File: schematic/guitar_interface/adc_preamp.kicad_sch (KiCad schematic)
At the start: 17 parts, among them U6 OPA4134

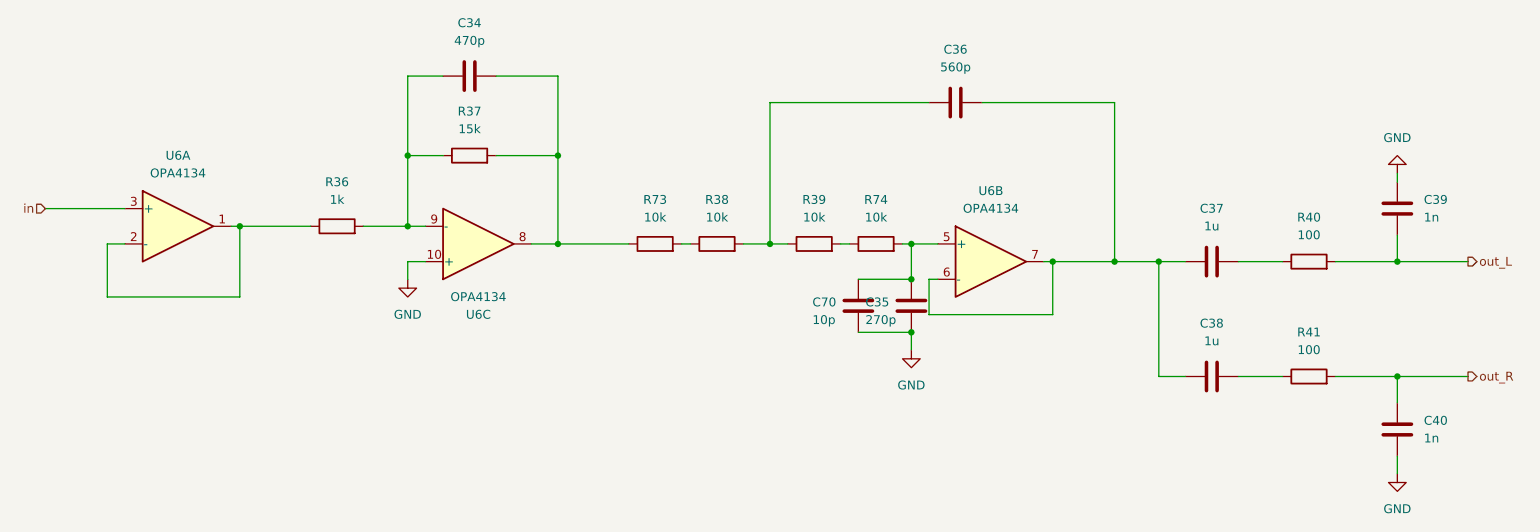
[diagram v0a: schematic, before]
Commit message: first scetch of audio pipeline and power supply layout
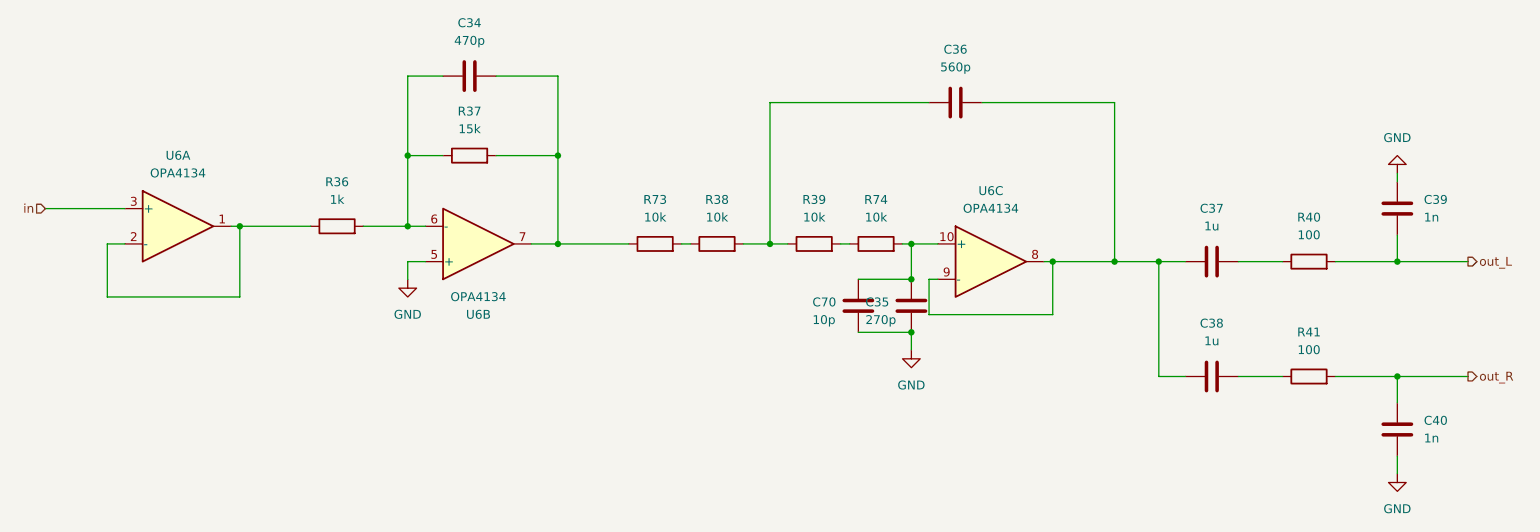
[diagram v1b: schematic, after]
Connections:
- net GND: now also U6.5 (+); no longer U6.10 (+)
- net at C34.1, R36.2, R37.1: now also U6.6 (-); no longer U6.9 (-)
- net at C35.1, C70.1, R74.2: now also U6.10 (+); no longer U6.5 (+)
- net at C34.2, R37.2, R73.1: now also U6.7; no longer U6.8
- net at C36.2, C37.1, C38.1: now also U6.8, U6.9 (-); no longer U6.6 (-), U6.7
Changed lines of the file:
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@@
 		(lib_id "Amplifier_Operational:OPA4134")
 		(at 180.34 93.98 0)
-		(unit 2)
+		(unit 3)
 		(exclude_from_sim no)
 		(in_bom yes)
@@
 				(path "/b77251ff-4eed-421f-8c84-983bb16b8e4c/3de8d587-ab61-418a-a618-c771618873d3"
 					(reference "U6")
-					(unit 2)
+					(unit 3)
 				)
 			)
@@
 		(at 106.68 91.44 0)
 		(mirror x)
-		(unit 3)
+		(unit 2)
 		(exclude_from_sim no)
 		(in_bom yes)
@@
 				(path "/b77251ff-4eed-421f-8c84-983bb16b8e4c/3de8d587-ab61-418a-a618-c771618873d3"
 					(reference "U6")
-					(unit 3)
-				)
-			)
+					(unit 2)
+				)
+			)
